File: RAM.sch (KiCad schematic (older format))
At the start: 158 parts, among them J2 JTAG_01x06, J3 Conn_01x03_Male, U10 W25Q128JVS, U11 TPS62823DLC, U12 TPS62823DLC, U13 TPS62823DLC, U14 TPS62823DLC, U15 TPS62823DLC, U16 TPS62823DLC, U2 XC7K160T-FFG676, U3 IS43TR16512B-125KBLI, U4 IS43TR16512B-125KBLI, U5 TPS51200DRC, U6 KSZ9031RNXCA, U7 TUSB1310ZAY, U8 TC358778XBG, U9 SiI9022A, Y1 ABM8G-25.000MHZ-18-D2Y-T, Y2 ABM8G-20.000MHZ-18-D2Y-T

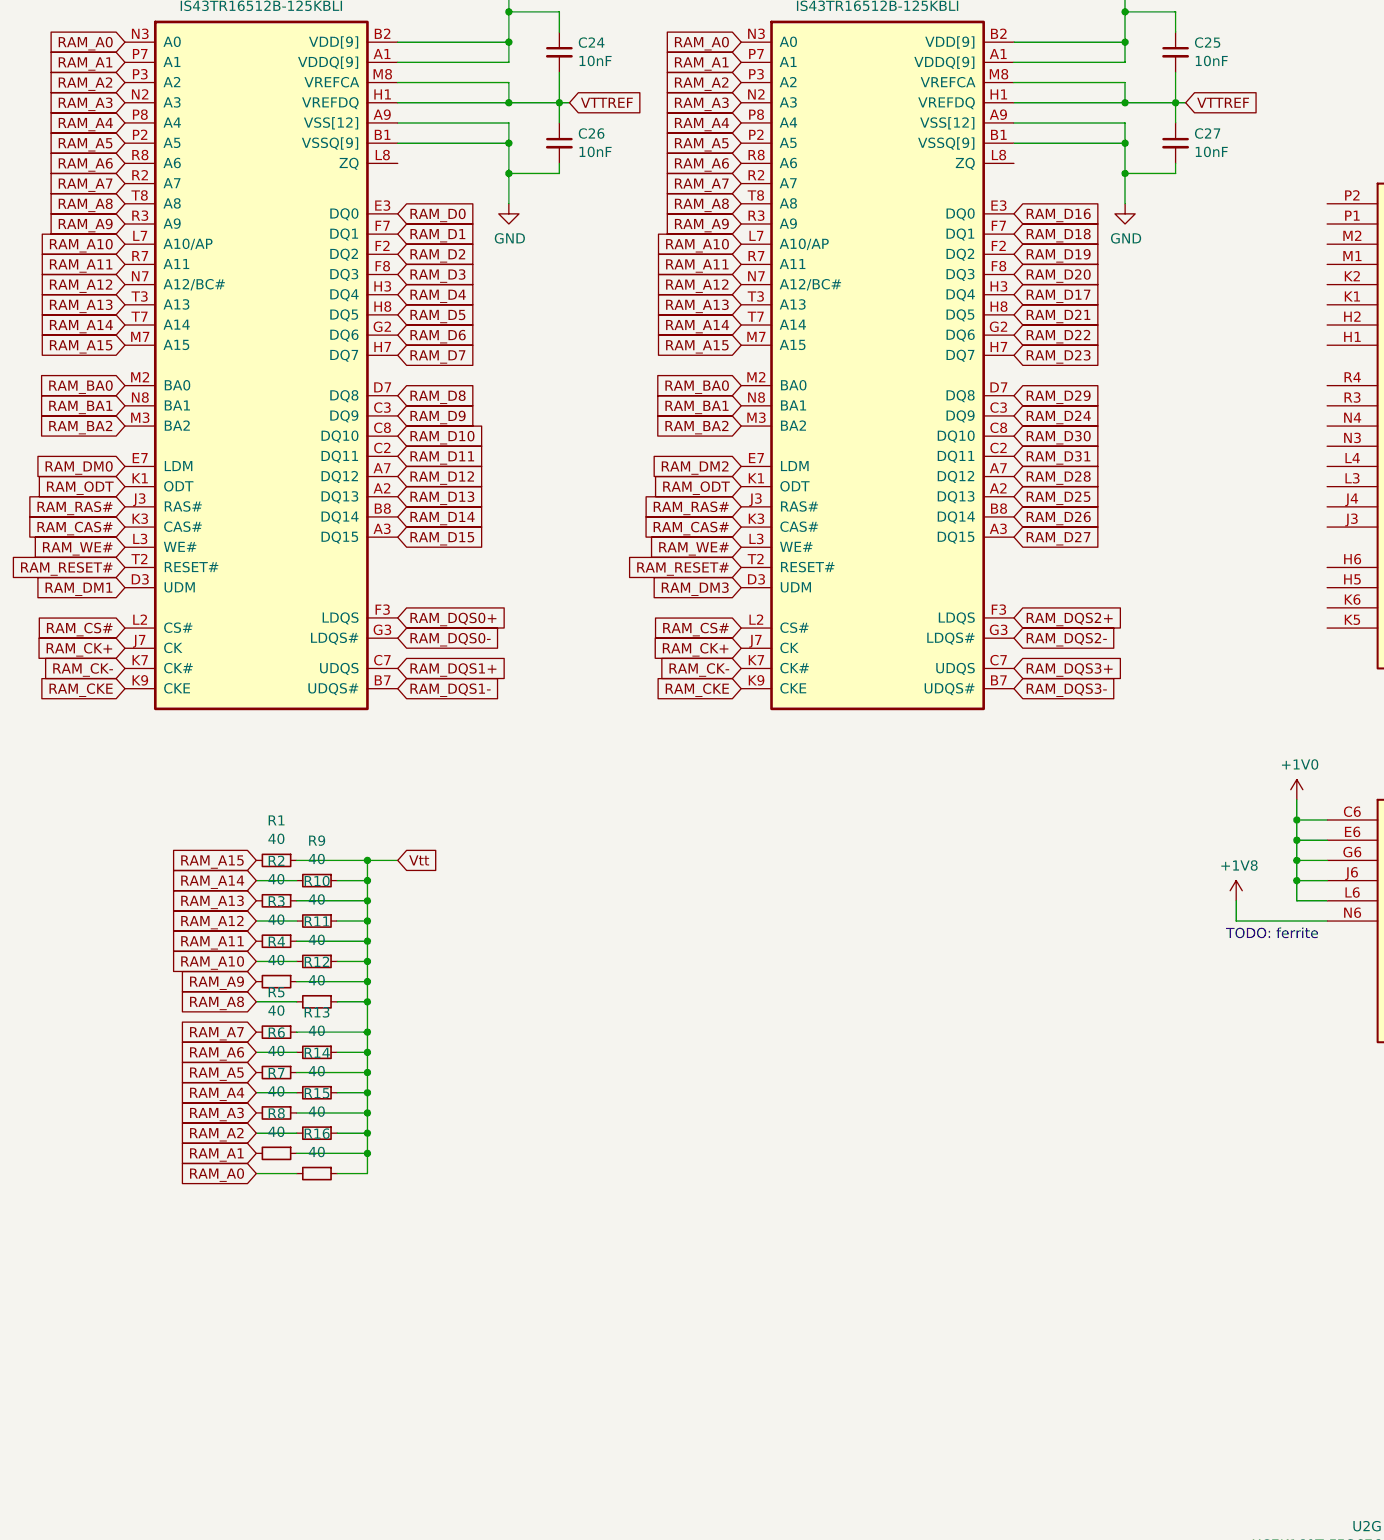
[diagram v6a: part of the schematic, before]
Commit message: ram bus termination
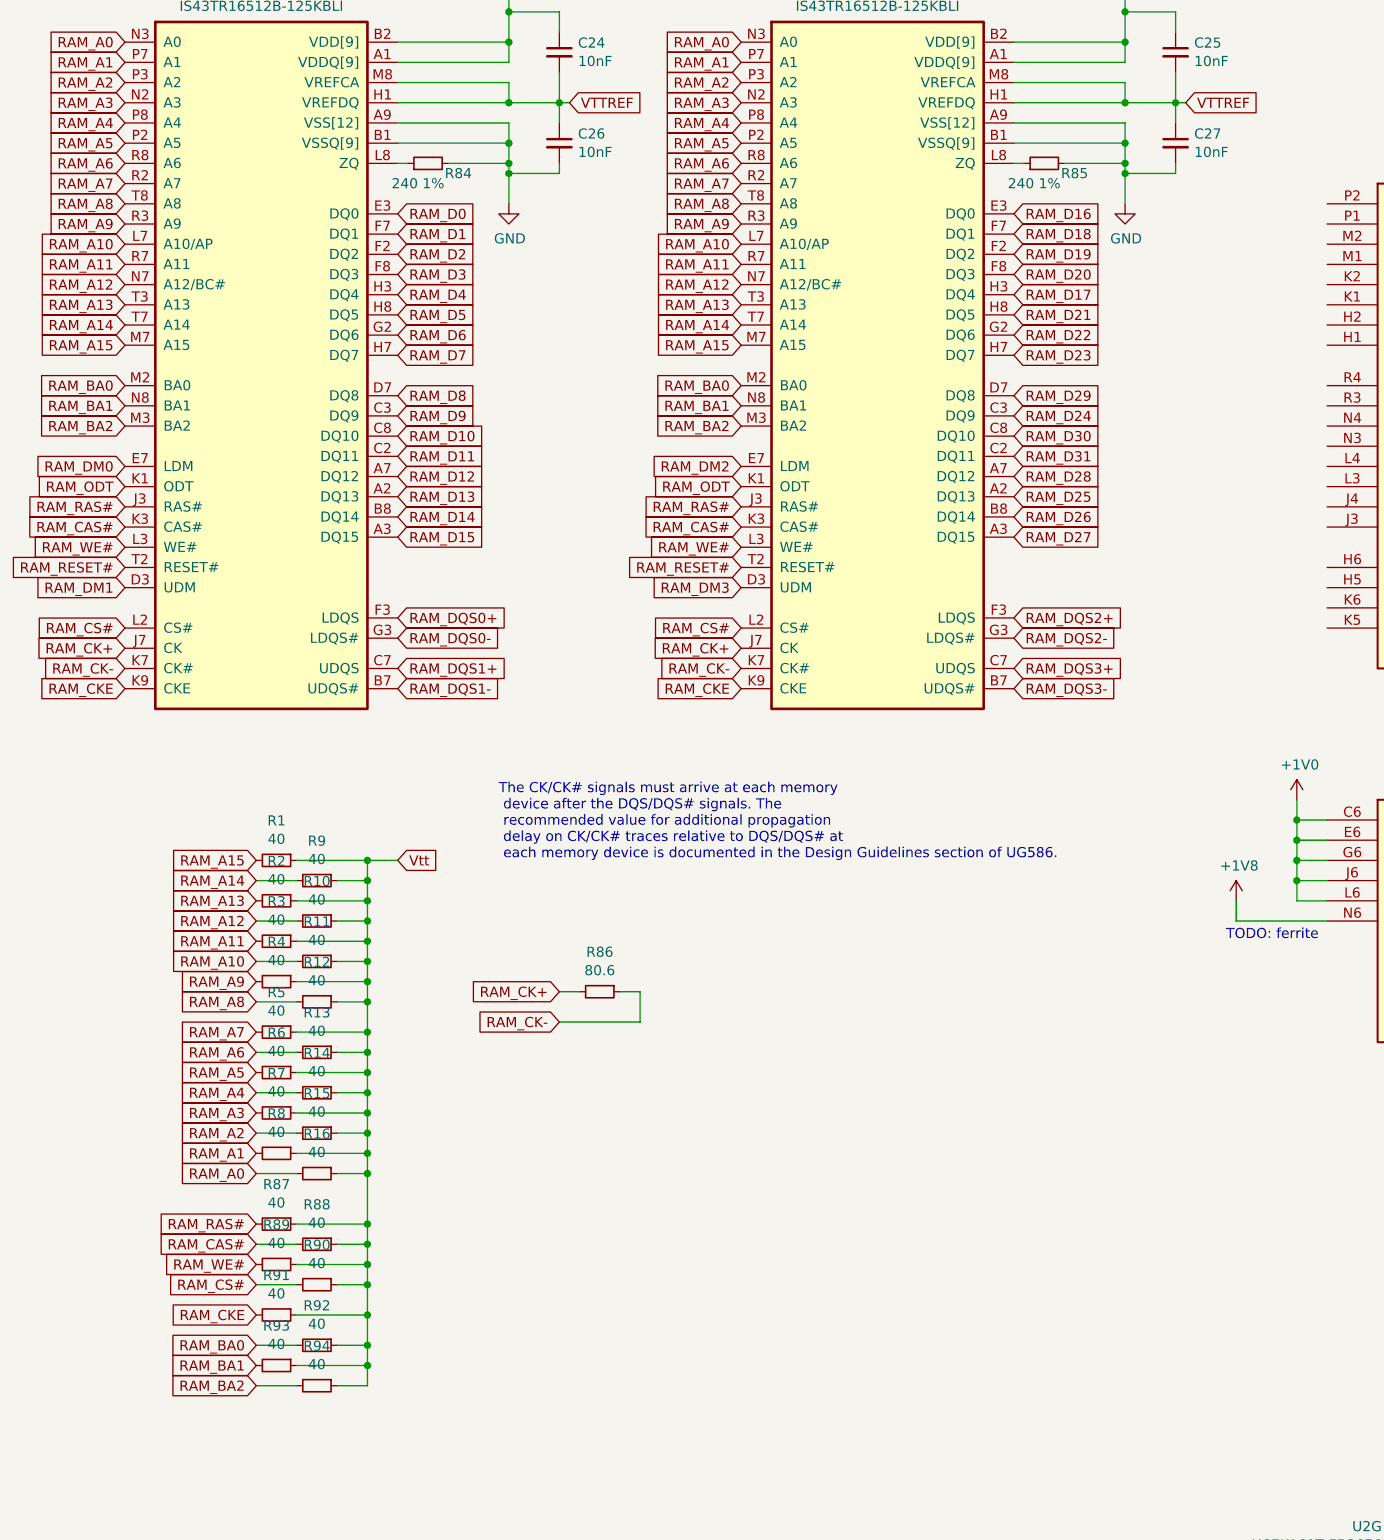
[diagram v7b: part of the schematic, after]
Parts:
- added R84, R85: 240 1%, Resistor_SMD:R_0402_1005Metric, symbol Device:R_Small
- added R86: 80.6, Resistor_SMD:R_0402_1005Metric, symbol Device:R_Small
- added R87, R88, R89, R90, R91, R92, R93, R94: 40, Resistor_SMD:R_0402_1005Metric, symbol Device:R_Small
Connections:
- net GND: now also R84.2, R85.2
- net RAM_BA0: now also R92.2
- net RAM_BA1: now also R93.2
- net RAM_BA2: now also R94.2
- net RAM_CAS#: now also R88.2
- net RAM_CK+: now also R86.2
- net RAM_CK-: now also R86.1
- net RAM_CKE: now also R91.2
- net RAM_CS#: now also R90.2
- net RAM_RAS#: now also R87.2
- net RAM_WE#: now also R89.2
- net Vtt: now also R87.1, R88.1, R89.1, R90.1, R91.1, R92.1, R93.1, R94.1
- net at U3.L8 (ZQ): now also R84.1
- net at U4.L8 (ZQ): now also R85.1
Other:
- note added: "The CK/CK# signals must arrive at each memory\n device after the DQS/DQS# signals. The\n recommended value for additional propagation\n delay on CK/CK# traces relative to DQS/DQS# at\n each memory device is documented in the Design Guidelines section of UG586."
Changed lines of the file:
@@
 Connection ~ 10350 9600
 Wire Wire Line
-	10350 9600 10350 9450
+	10350 9600 10350 9550
 Text GLabel 13700 9250 2    50   Input ~ 0
 VTTREF
@@
 Connection ~ 13400 9600
 Wire Wire Line
-	13400 9600 13400 9450
+	13400 9600 13400 9550
 Wire Wire Line
 	12850 9250 13400 9250
@@
 Text GLabel 6050 10500 2    50   Input ~ 0
 RAM_D0
+Text Notes 10300 13000 0    50   ~ 0
+The CK/CK# signals must arrive at each memory\n device after the DQS/DQS# signals. The\n recommended value for additional propagation\n delay on CK/CK# traces relative to DQS/DQS# at\n each memory device is documented in the Design Guidelines section of UG586.
+Text GLabel 9100 14800 0    50   Input ~ 0
+RAM_RAS#
+Text GLabel 9100 14900 0    50   Input ~ 0
+RAM_CAS#
+Text GLabel 9100 15000 0    50   Input ~ 0
+RAM_WE#
+Text GLabel 9100 15400 0    50   Input ~ 0
+RAM_BA0
+Text GLabel 9100 15500 0    50   Input ~ 0
+RAM_BA1
+Text GLabel 9100 15600 0    50   Input ~ 0
+RAM_BA2
+Text GLabel 9100 15100 0    50   Input ~ 0
+RAM_CS#
+Text GLabel 9100 15250 0    50   Input ~ 0
+RAM_CKE
+$Comp
+L Device:R_Small R84
+U 1 1 62E50D67
+P 9950 9550
+F 0 "R84" V 9900 9400 50  0000 C CNN
+F 1 "240 1%" V 9850 9600 50  0000 C CNN
+F 2 "Resistor_SMD:R_0402_1005Metric" H 9950 9550 50  0001 C CNN
+F 3 "~" H 9950 9550 50  0001 C CNN
+	1    9950 9550
+	0    -1   -1   0
+$EndComp
+Wire Wire Line
+	9850 9550 9800 9550
+Wire Wire Line
+	10050 9550 10350 9550
+Connection ~ 10350 9550
+Wire Wire Line
+	10350 9550 10350 9450
+$Comp
+L Device:R_Small R85
+U 1 1 6317E834
+P 13000 9550
+F 0 "R85" V 12950 9400 50  0000 C CNN
+F 1 "240 1%" V 12900 9600 50  0000 C CNN
+F 2 "Resistor_SMD:R_0402_1005Metric" H 13000 9550 50  0001 C CNN
+F 3 "~" H 13000 9550 50  0001 C CNN
+	1    13000 9550
+	0    -1   -1   0
+$EndComp
+Wire Wire Line
+	12900 9550 12850 9550
+Wire Wire Line
+	13100 9550 13400 9550
+Connection ~ 13400 9550
+Wire Wire Line
+	13400 9550 13400 9450
+$Comp
+L Device:R_Small R87
+U 1 1 634AF5EB
+P 9200 14800
+F 0 "R87" V 9004 14800 50  0000 C CNN
+F 1 "40" V 9095 14800 50  0000 C CNN
+F 2 "Resistor_SMD:R_0402_1005Metric" H 9200 14800 50  0001 C CNN
+F 3 "~" H 9200 14800 50  0001 C CNN
+	1    9200 14800
+	0    1    1    0
+$EndComp
+$Comp
+L Device:R_Small R88
+U 1 1 634AF8A5
+P 9400 14900
+F 0 "R88" V 9204 14900 50  0000 C CNN
+F 1 "40" V 9295 14900 50  0000 C CNN
+F 2 "Resistor_SMD:R_0402_1005Metric" H 9400 14900 50  0001 C CNN
+F 3 "~" H 9400 14900 50  0001 C CNN
+	1    9400 14900
+	0    1    1    0
+$EndComp
+$Comp
+L Device:R_Small R89
+U 1 1 634AFAD6
+P 9200 15000
+F 0 "R89" V 9004 15000 50  0000 C CNN
+F 1 "40" V 9095 15000 50  0000 C CNN
+F 2 "Resistor_SMD:R_0402_1005Metric" H 9200 15000 50  0001 C CNN
+F 3 "~" H 9200 15000 50  0001 C CNN
+	1    9200 15000
+	0    1    1    0
+$EndComp
+$Comp
+L Device:R_Small R90
+U 1 1 634AFCD4
+P 9400 15100
+F 0 "R90" V 9204 15100 50  0000 C CNN
+F 1 "40" V 9295 15100 50  0000 C CNN
+F 2 "Resistor_SMD:R_0402_1005Metric" H 9400 15100 50  0001 C CNN
+F 3 "~" H 9400 15100 50  0001 C CNN
+	1    9400 15100
+	0    1    1    0
+$EndComp
+$Comp
+L Device:R_Small R91
+U 1 1 634AFFD1
+P 9200 15250
+F 0 "R91" V 9004 15250 50  0000 C CNN
+F 1 "40" V 9095 15250 50  0000 C CNN
+F 2 "Resistor_SMD:R_0402_1005Metric" H 9200 15250 50  0001 C CNN
+F 3 "~" H 9200 15250 50  0001 C CNN
+	1    9200 15250
+	0    1    1    0
+$EndComp
+$Comp
+L Device:R_Small R92
+U 1 1 634B044E
+P 9400 15400
+F 0 "R92" V 9204 15400 50  0000 C CNN
+F 1 "40" V 9295 15400 50  0000 C CNN
+F 2 "Resistor_SMD:R_0402_1005Metric" H 9400 15400 50  0001 C CNN
+F 3 "~" H 9400 15400 50  0001 C CNN
+	1    9400 15400
+	0    1    1    0
+$EndComp
+$Comp
+L Device:R_Small R93
+U 1 1 634B059A
+P 9200 15500
+F 0 "R93" V 9004 15500 50  0000 C CNN
+F 1 "40" V 9095 15500 50  0000 C CNN
+F 2 "Resistor_SMD:R_0402_1005Metric" H 9200 15500 50  0001 C CNN
+F 3 "~" H 9200 15500 50  0001 C CNN
+	1    9200 15500
+	0    1    1    0
+$EndComp
+$Comp
+L Device:R_Small R94
+U 1 1 634B06E1
+P 9400 15600
+F 0 "R94" V 9204 15600 50  0000 C CNN
+F 1 "40" V 9295 15600 50  0000 C CNN
+F 2 "Resistor_SMD:R_0402_1005Metric" H 9400 15600 50  0001 C CNN
+F 3 "~" H 9400 15600 50  0001 C CNN
+	1    9400 15600
+	0    1    1    0
+$EndComp
+Wire Wire Line
+	9300 14900 9100 14900
+Wire Wire Line
+	9100 15100 9300 15100
+Wire Wire Line
+	9100 15400 9300 15400
+Wire Wire Line
+	9100 15600 9300 15600
+Wire Wire Line
+	9300 14800 9650 14800
+Wire Wire Line
+	9650 14800 9650 14550
+Connection ~ 9650 14550
+Wire Wire Line
+	9500 14900 9650 14900
+Wire Wire Line
+	9650 14900 9650 14800
+Connection ~ 9650 14800
+Wire Wire Line
+	9300 15000 9650 15000
+Wire Wire Line
+	9650 15000 9650 14900
+Connection ~ 9650 14900
+Wire Wire Line
+	9500 15100 9650 15100
+Wire Wire Line
+	9650 15100 9650 15000
+Connection ~ 9650 15000
+Wire Wire Line
+	9300 15250 9650 15250
+Wire Wire Line
+	9650 15250 9650 15100
+Connection ~ 9650 15100
+Wire Wire Line
+	9500 15400 9650 15400
+Wire Wire Line
+	9650 15400 9650 15250
+Connection ~ 9650 15250
+Wire Wire Line
+	9300 15500 9650 15500
+Wire Wire Line
+	9650 15500 9650 15400
+Connection ~ 9650 15400
+Wire Wire Line
+	9500 15600 9650 15600
+Wire Wire Line
+	9650 15600 9650 15500
+Connection ~ 9650 15500
+$Comp
+L Device:R_Small R86
+U 1 1 649C1968
+P 10800 13650
+F 0 "R86" V 10604 13650 50  0000 C CNN
+F 1 "80.6" V 10695 13650 50  0000 C CNN
+F 2 "Resistor_SMD:R_0402_1005Metric" H 10800 13650 50  0001 C CNN
+F 3 "~" H 10800 13650 50  0001 C CNN
+	1    10800 13650
+	0    1    1    0
+$EndComp
+Text GLabel 10600 13650 0    50   Input ~ 0
+RAM_CK+
+Text GLabel 10600 13800 0    50   Input ~ 0
+RAM_CK-
+Wire Wire Line
+	10600 13650 10700 13650
+Wire Wire Line
+	10600 13800 11000 13800
+Wire Wire Line
+	11000 13800 11000 13650
+Wire Wire Line
+	11000 13650 10900 13650
 $EndSCHEMATC

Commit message: DSI and some USB routing
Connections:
- net DISP2_DE: now also U2.AA15 (IO_L7N_T1_32); no longer U2.AD20 (IO_L15P_T2_DQS_32)
- net DISP2_HS: now also U2.AB15 (IO_L10N_T1_32); no longer U2.AB17 (IO_L14P_T2_SRCC_32)
- net DISP2_RGB0: now also U2.AF15 (IO_L2N_T0_32); no longer U2.AC16 (IO_L12N_T1_MRCC_32)
- net DISP2_RGB1: now also U2.AF14 (IO_L2P_T0_32); no longer U2.AB16 (IO_L12P_T1_MRCC_32)
- net DISP2_RGB10: now also U2.AD16 (IO_L6P_T0_32); no longer U2.AA15 (IO_L7N_T1_32)
- net DISP2_RGB11: now also U2.AF19 (IO_L5P_T0_32); no longer U2.AA14 (IO_L7P_T1_32)
- net DISP2_RGB12: now also U2.AC16 (IO_L12N_T1_MRCC_32); no longer U2.AE16 (IO_L6N_T0_VREF_32)
- net DISP2_RGB13: now also U2.AD14 (IO_L8N_T1_32); no longer U2.AD16 (IO_L6P_T0_32)
- net DISP2_RGB14: now also U2.AC17 (IO_L14N_T2_SRCC_32); no longer U2.AF20 (IO_L5N_T0_32)
- net DISP2_RGB15: now also U2.AC14 (IO_L8P_T1_32); no longer U2.AF19 (IO_L5P_T0_32)
- net DISP2_RGB16: now also U2.AB14 (IO_L10P_T1_32); no longer U2.AE15 (IO_L4N_T0_32)
- net DISP2_RGB17: now also U2.AA17 (IO_L11P_T1_SRCC_32); no longer U2.AD15 (IO_L4P_T0_32)
- net DISP2_RGB18: now also U2.Y15 (IO_L9P_T1_DQS_32); no longer U2.AF18 (IO_L3N_T0_DQS_32)
- net DISP2_RGB19: now also U2.AA18 (IO_L11N_T1_SRCC_32); no longer U2.AE18 (IO_L3P_T0_DQS_32)
- net DISP2_RGB2: now also U2.AE16 (IO_L6N_T0_VREF_32); no longer U2.AA18 (IO_L11N_T1_SRCC_32)
- net DISP2_RGB20: now also U2.Y16 (IO_L9N_T1_DQS_32); no longer U2.AF15 (IO_L2N_T0_32)
- net DISP2_RGB21: now also U2.AB17 (IO_L14P_T2_SRCC_32); no longer U2.AF14 (IO_L2P_T0_32)
- net DISP2_RGB22: now also U2.AF20 (IO_L5N_T0_32); no longer U2.AF17 (IO_L1N_T0_32)
- net DISP2_RGB23: now also U2.AD20 (IO_L15P_T2_DQS_32); no longer U2.AE17 (IO_L1P_T0_32)
- net DISP2_RGB3: now also U2.AE15 (IO_L4N_T0_32); no longer U2.AA17 (IO_L11P_T1_SRCC_32)
- net DISP2_RGB4: now also U2.AE17 (IO_L1P_T0_32); no longer U2.AB15 (IO_L10N_T1_32)
- net DISP2_RGB5: now also U2.AF17 (IO_L1N_T0_32); no longer U2.AB14 (IO_L10P_T1_32)
- net DISP2_RGB6: now also U2.AA14 (IO_L7P_T1_32); no longer U2.Y16 (IO_L9N_T1_DQS_32)
- net DISP2_RGB7: now also U2.AF18 (IO_L3N_T0_DQS_32); no longer U2.Y15 (IO_L9P_T1_DQS_32)
- net DISP2_RGB8: now also U2.AD15 (IO_L4P_T0_32); no longer U2.AD14 (IO_L8N_T1_32)
- net DISP2_RGB9: now also U2.AE18 (IO_L3P_T0_DQS_32); no longer U2.AC14 (IO_L8P_T1_32)
- net DISP2_VS: now also U2.AB16 (IO_L12P_T1_MRCC_32); no longer U2.AC17 (IO_L14N_T2_SRCC_32)
- no-connect marks 22 -> 23
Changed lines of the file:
@@
 Text GLabel 12800 5000 0    50   Output ~ 0
 DISP1_DE
-Text GLabel 16800 4500 2    50   Input ~ 0
+Text GLabel 16800 2500 2    50   Input ~ 0
 DISP2_RGB0
-Text GLabel 16800 4400 2    50   Input ~ 0
+Text GLabel 16800 2400 2    50   Input ~ 0
 DISP2_RGB1
-Text GLabel 16800 4300 2    50   Input ~ 0
+Text GLabel 16800 3300 2    50   Input ~ 0
 DISP2_RGB2
-Text GLabel 16800 4200 2    50   Input ~ 0
+Text GLabel 16800 2900 2    50   Input ~ 0
 DISP2_RGB3
-Text GLabel 16800 4100 2    50   Input ~ 0
+Text GLabel 16800 2200 2    50   Input ~ 0
 DISP2_RGB4
-Text GLabel 16800 4000 2    50   Input ~ 0
+Text GLabel 16800 2300 2    50   Input ~ 0
 DISP2_RGB5
-Text GLabel 16800 3900 2    50   Input ~ 0
+Text GLabel 16800 3400 2    50   Input ~ 0
 DISP2_RGB6
-Text GLabel 16800 3800 2    50   Input ~ 0
+Text GLabel 16800 2700 2    50   Input ~ 0
 DISP2_RGB7
-Text GLabel 16800 3700 2    50   Input ~ 0
+Text GLabel 16800 2800 2    50   Input ~ 0
 DISP2_RGB8
-Text GLabel 16800 3600 2    50   Input ~ 0
-DISP2_RGB9
-Text GLabel 16800 3500 2    50   Input ~ 0
+Text GLabel 16800 3200 2    50   Input ~ 0
 DISP2_RGB10
-Text GLabel 16800 3400 2    50   Input ~ 0
+Text GLabel 16800 3000 2    50   Input ~ 0
 DISP2_RGB11
-Text GLabel 16800 3300 2    50   Input ~ 0
+Text GLabel 16800 4500 2    50   Input ~ 0
 DISP2_RGB12
-Text GLabel 16800 3200 2    50   Input ~ 0
+Text GLabel 16800 3700 2    50   Input ~ 0
 DISP2_RGB13
-Text GLabel 16800 3100 2    50   Input ~ 0
+Text GLabel 16800 4900 2    50   Input ~ 0
 DISP2_RGB14
-Text GLabel 16800 3000 2    50   Input ~ 0
+Text GLabel 16800 3600 2    50   Input ~ 0
 DISP2_RGB15
-Text GLabel 16800 2900 2    50   Input ~ 0
+Text GLabel 16800 4000 2    50   Input ~ 0
 DISP2_RGB16
-Text GLabel 16800 2800 2    50   Input ~ 0
+Text GLabel 16800 4200 2    50   Input ~ 0
 DISP2_RGB17
-Text GLabel 16800 2700 2    50   Input ~ 0
-DISP2_RGB18
-Text GLabel 16800 2600 2    50   Input ~ 0
+Text GLabel 16800 4300 2    50   Input ~ 0
 DISP2_RGB19
-Text GLabel 16800 2500 2    50   Input ~ 0
+Text GLabel 16800 3900 2    50   Input ~ 0
 DISP2_RGB20
-Text GLabel 16800 2400 2    50   Input ~ 0
+Text GLabel 16800 4800 2    50   Input ~ 0
 DISP2_RGB21
-Text GLabel 16800 2300 2    50   Input ~ 0
+Text GLabel 16800 3100 2    50   Input ~ 0
 DISP2_RGB22
-Text GLabel 16800 2200 2    50   Input ~ 0
+Text GLabel 16800 5000 2    50   Input ~ 0
 DISP2_RGB23
-Text GLabel 16800 4900 2    50   Output ~ 0
+Text GLabel 16800 4400 2    50   Output ~ 0
 DISP2_VS
-Text GLabel 16800 4800 2    50   Output ~ 0
+Text GLabel 16800 4100 2    50   Output ~ 0
 DISP2_HS
-Text GLabel 16800 5000 2    50   Output ~ 0
+Text GLabel 16800 3500 2    50   Output ~ 0
 DISP2_DE
 Text GLabel 17750 11650 2    50   Input ~ 0
@@
 Wire Wire Line
 	11000 13650 10900 13650
+NoConn ~ 16800 5100
+Text GLabel 16800 2600 2    50   Input ~ 0
+DISP2_RGB9
+Text GLabel 16800 3800 2    50   Input ~ 0
+DISP2_RGB18
 $EndSCHEMATC
